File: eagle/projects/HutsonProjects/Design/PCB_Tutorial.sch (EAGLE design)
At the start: 1 part

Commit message: adding parts
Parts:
- added C1: 0.1uF, SparkFun-Capacitors:0.1UF-0603-25V-(+80/-20%)
- added J1: POWER_JACKPTH_BREAD, SparkFun-Connectors:POWER_JACKPTH_BREAD
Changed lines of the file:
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@@
 <parts>
 <part name="FRAME1" library="SparkFun-Aesthetics" deviceset="FRAME-LETTER" device=""/>
+<part name="J1" library="SparkFun-Connectors" deviceset="POWER_JACK" device="PTH_BREAD"/>
+<part name="C1" library="SparkFun-Capacitors" deviceset="0.1UF" device="-0603-25V-(+80/-20%)" value="0.1uF"/>
+<part name="SUPPLY1" library="SparkFun-PowerSymbols" deviceset="VCC" device=""/>
+<part name="GND1" library="SparkFun-PowerSymbols" deviceset="GND" device=""/>
+<part name="GND2" library="SparkFun-PowerSymbols" deviceset="GND" device=""/>
 </parts>
 <sheets>
@@
 <attribute name="REV" x="53.34" y="-51.816" size="2.7432" layer="94" font="vector"/>
 </instance>
+<instance part="J1" gate="G$1" x="-162.56" y="81.28" smashed="yes">
+<attribute name="VALUE" x="-172.72" y="91.44" size="1.778" layer="96" font="vector"/>
+<attribute name="NAME" x="-172.72" y="81.28" size="1.778" layer="95" font="vector"/>
+</instance>
+<instance part="C1" gate="G$1" x="-127" y="81.28" smashed="yes">
+<attribute name="NAME" x="-125.476" y="84.201" size="1.778" layer="95" font="vector"/>
+<attribute name="VALUE" x="-125.476" y="79.121" size="1.778" layer="96" font="vector"/>
+</instance>
+<instance part="SUPPLY1" gate="G$1" x="-132.08" y="101.6" smashed="yes">
+<attribute name="VALUE" x="-132.08" y="104.394" size="1.778" layer="96" align="bottom-center"/>
+</instance>
+<instance part="GND1" gate="1" x="-160.02" y="66.04" smashed="yes">
+<attribute name="VALUE" x="-160.02" y="65.786" size="1.778" layer="96" align="top-center"/>
+</instance>
+<instance part="GND2" gate="1" x="-144.78" y="66.04" smashed="yes">
+<attribute name="VALUE" x="-144.78" y="65.786" size="1.778" layer="96" align="top-center"/>
+</instance>
 </instances>

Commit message: adding parts
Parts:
- added C2: 0.1uF, SparkFun-Capacitors:0.1UF-KIT-EZ-50V-20%
- added D1, D2, D3: (no value), SparkFun-LED:LED5MM
- added R1, R2, R3, R4: (no value), SparkFun-Resistors:RESISTORAXIAL-0.3
- added U1: 328P, SparkFun-IC-Microcontroller:ATMEGA328P_PDIP
- C1: device SparkFun-Capacitors:0.1UF-0603-25V-(+80/-20%) -> SparkFun-Capacitors:0.1UF-KIT-EZ-50V-20%
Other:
- moved on the sheet: C1
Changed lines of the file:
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@@
 <part name="FRAME1" library="SparkFun-Aesthetics" deviceset="FRAME-LETTER" device=""/>
 <part name="J1" library="SparkFun-Connectors" deviceset="POWER_JACK" device="PTH_BREAD"/>
-<part name="C1" library="SparkFun-Capacitors" deviceset="0.1UF" device="-0603-25V-(+80/-20%)" value="0.1uF"/>
 <part name="SUPPLY1" library="SparkFun-PowerSymbols" deviceset="VCC" device=""/>
 <part name="GND1" library="SparkFun-PowerSymbols" deviceset="GND" device=""/>
 <part name="GND2" library="SparkFun-PowerSymbols" deviceset="GND" device=""/>
+<part name="U1" library="SparkFun-IC-Microcontroller" deviceset="ATMEGA328P_PDIP" device="" value="328P"/>
+<part name="R1" library="SparkFun-Resistors" deviceset="RESISTOR" device="AXIAL-0.3" value=" "/>
+<part name="R2" library="SparkFun-Resistors" deviceset="RESISTOR" device="AXIAL-0.3" value=" "/>
+<part name="R3" library="SparkFun-Resistors" deviceset="RESISTOR" device="AXIAL-0.3" value=" "/>
+<part name="R4" library="SparkFun-Resistors" deviceset="RESISTOR" device="AXIAL-0.3" value=" "/>
+<part name="C1" library="SparkFun-Capacitors" deviceset="0.1UF" device="-KIT-EZ-50V-20%" value="0.1uF"/>
+<part name="D1" library="SparkFun-LED" deviceset="LED" device="5MM"/>
+<part name="D2" library="SparkFun-LED" deviceset="LED" device="5MM"/>
+<part name="D3" library="SparkFun-LED" deviceset="LED" device="5MM"/>
+<part name="C2" library="SparkFun-Capacitors" deviceset="0.1UF" device="-KIT-EZ-50V-20%" value="0.1uF"/>
 </parts>
 <sheets>
@@
 <attribute name="NAME" x="-172.72" y="81.28" size="1.778" layer="95" font="vector"/>
 </instance>
-<instance part="C1" gate="G$1" x="-127" y="81.28" smashed="yes">
-<attribute name="NAME" x="-125.476" y="84.201" size="1.778" layer="95" font="vector"/>
-<attribute name="VALUE" x="-125.476" y="79.121" size="1.778" layer="96" font="vector"/>
-</instance>
 <instance part="SUPPLY1" gate="G$1" x="-132.08" y="101.6" smashed="yes">
 <attribute name="VALUE" x="-132.08" y="104.394" size="1.778" layer="96" align="bottom-center"/>
@@
 <attribute name="VALUE" x="-144.78" y="65.786" size="1.778" layer="96" align="top-center"/>
 </instance>
+<instance part="U1" gate="U1" x="-88.9" y="60.96" smashed="yes">
+<attribute name="NAME" x="-106.68" y="89.662" size="1.778" layer="95"/>
+<attribute name="VALUE" x="-106.68" y="22.86" size="1.778" layer="96"/>
+</instance>
+<instance part="R1" gate="G$1" x="-48.26" y="93.98" smashed="yes">
+<attribute name="NAME" x="-48.26" y="95.504" size="1.778" layer="95" font="vector" align="bottom-center"/>
+<attribute name="VALUE" x="-48.26" y="92.456" size="1.778" layer="96" font="vector" align="top-center"/>
+</instance>
+<instance part="R2" gate="G$1" x="-25.4" y="93.98" smashed="yes">
+<attribute name="NAME" x="-25.4" y="95.504" size="1.778" layer="95" font="vector" align="bottom-center"/>
+<attribute name="VALUE" x="-25.4" y="92.456" size="1.778" layer="96" font="vector" align="top-center"/>
+</instance>
+<instance part="R3" gate="G$1" x="-17.78" y="81.28" smashed="yes">
+<attribute name="NAME" x="-17.78" y="82.804" size="1.778" layer="95" font="vector" align="bottom-center"/>
+<attribute name="VALUE" x="-17.78" y="79.756" size="1.778" layer="96" font="vector" align="top-center"/>
+</instance>
+<instance part="R4" gate="G$1" x="12.7" y="101.6" smashed="yes">
+<attribute name="NAME" x="12.7" y="103.124" size="1.778" layer="95" font="vector" align="bottom-center"/>
+<attribute name="VALUE" x="12.7" y="100.076" size="1.778" layer="96" font="vector" align="top-center"/>
+</instance>
+<instance part="C1" gate="G$1" x="-129.54" y="73.66" smashed="yes">
+<attribute name="NAME" x="-128.016" y="76.581" size="1.778" layer="95" font="vector"/>
+<attribute name="VALUE" x="-128.016" y="71.501" size="1.778" layer="96" font="vector"/>
+</instance>
+<instance part="D1" gate="D1" x="-22.86" y="45.72" smashed="yes">
+<attribute name="NAME" x="-26.289" y="41.148" size="1.778" layer="95" font="vector" rot="R90"/>
+<attribute name="VALUE" x="-20.955" y="41.148" size="1.778" layer="96" font="vector" rot="R90" align="top-left"/>
+</instance>
+<instance part="D2" gate="D1" x="-10.16" y="45.72" smashed="yes">
+<attribute name="NAME" x="-13.589" y="41.148" size="1.778" layer="95" font="vector" rot="R90"/>
+<attribute name="VALUE" x="-8.255" y="41.148" size="1.778" layer="96" font="vector" rot="R90" align="top-left"/>
+</instance>
+<instance part="D3" gate="D1" x="0" y="48.26" smashed="yes">
+<attribute name="NAME" x="-3.429" y="43.688" size="1.778" layer="95" font="vector" rot="R90"/>
+<attribute name="VALUE" x="1.905" y="43.688" size="1.778" layer="96" font="vector" rot="R90" align="top-left"/>
+</instance>
+<instance part="C2" gate="G$1" x="-121.92" y="93.98" smashed="yes">
+<attribute name="NAME" x="-120.396" y="96.901" size="1.778" layer="95" font="vector"/>
+<attribute name="VALUE" x="-120.396" y="91.821" size="1.778" layer="96" font="vector"/>
+</instance>
 </instances>

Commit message: adding parts
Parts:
- added J2: (no value), SparkFun-Connectors:CONN_08"
- added J3: AVR_SPI_PROG_3X2PTH, SparkFun-Connectors:AVR_SPI_PROG_3X2PTH
- added J4: 6_PIN_SERIAL_CABLEPTH, SparkFun-Connectors:6_PIN_SERIAL_CABLEPTH
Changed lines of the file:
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@@
 <part name="D3" library="SparkFun-LED" deviceset="LED" device="5MM"/>
 <part name="C2" library="SparkFun-Capacitors" deviceset="0.1UF" device="-KIT-EZ-50V-20%" value="0.1uF"/>
+<part name="SUPPLY2" library="SparkFun-PowerSymbols" deviceset="VCC" device=""/>
+<part name="GND3" library="SparkFun-PowerSymbols" deviceset="GND" device=""/>
+<part name="SUPPLY3" library="SparkFun-PowerSymbols" deviceset="VCC" device=""/>
+<part name="GND4" library="SparkFun-PowerSymbols" deviceset="GND" device=""/>
+<part name="GND5" library="SparkFun-PowerSymbols" deviceset="GND" device=""/>
+<part name="GND6" library="SparkFun-PowerSymbols" deviceset="GND" device=""/>
+<part name="J2" library="SparkFun-Connectors" deviceset="CONN_08" device="&quot;"/>
+<part name="J3" library="SparkFun-Connectors" deviceset="AVR_SPI_PROG_3X2" device="PTH"/>
+<part name="J4" library="SparkFun-Connectors" deviceset="6_PIN_SERIAL_CABLE" device="PTH"/>
+<part name="SUPPLY4" library="SparkFun-PowerSymbols" deviceset="VCC" device=""/>
+<part name="SUPPLY5" library="SparkFun-PowerSymbols" deviceset="VCC" device=""/>
+<part name="GND7" library="SparkFun-PowerSymbols" deviceset="GND" device=""/>
+<part name="GND8" library="SparkFun-PowerSymbols" deviceset="GND" device=""/>
 </parts>
 <sheets>
@@
 <attribute name="VALUE" x="-120.396" y="91.821" size="1.778" layer="96" font="vector"/>
 </instance>
+<instance part="SUPPLY2" gate="G$1" x="-106.68" y="104.14" smashed="yes">
+<attribute name="VALUE" x="-106.68" y="106.934" size="1.778" layer="96" align="bottom-center"/>
+</instance>
+<instance part="GND3" gate="1" x="-154.94" y="40.64" smashed="yes">
+<attribute name="VALUE" x="-154.94" y="40.386" size="1.778" layer="96" align="top-center"/>
+</instance>
+<instance part="SUPPLY3" gate="G$1" x="-96.52" y="104.14" smashed="yes">
+<attribute name="VALUE" x="-96.52" y="106.934" size="1.778" layer="96" align="bottom-center"/>
+</instance>
+<instance part="GND4" gate="1" x="-147.32" y="48.26" smashed="yes">
+<attribute name="VALUE" x="-147.32" y="48.006" size="1.778" layer="96" align="top-center"/>
+</instance>
+<instance part="GND5" gate="1" x="-137.16" y="48.26" smashed="yes">
+<attribute name="VALUE" x="-137.16" y="48.006" size="1.778" layer="96" align="top-center"/>
+</instance>
+<instance part="GND6" gate="1" x="-142.24" y="40.64" smashed="yes">
+<attribute name="VALUE" x="-142.24" y="40.386" size="1.778" layer="96" align="top-center"/>
+</instance>
+<instance part="J2" gate="G$1" x="40.64" y="83.82" smashed="yes" rot="R180">
+<attribute name="VALUE" x="45.72" y="96.266" size="1.778" layer="96" font="vector" rot="R180"/>
+<attribute name="NAME" x="45.72" y="70.612" size="1.778" layer="95" font="vector" rot="R180"/>
+</instance>
+<instance part="J3" gate="G$1" x="33.02" y="48.26" smashed="yes" rot="R180">
+<attribute name="NAME" x="38.1" y="42.672" size="1.778" layer="95" font="vector" rot="R180"/>
+<attribute name="VALUE" x="38.1" y="55.626" size="1.778" layer="96" font="vector" rot="R180"/>
+</instance>
+<instance part="J4" gate="G$1" x="50.8" y="25.4" smashed="yes" rot="R180">
+<attribute name="VALUE" x="55.88" y="35.306" size="1.778" layer="96" font="vector" rot="R180"/>
+<attribute name="NAME" x="55.88" y="14.732" size="1.778" layer="95" font="vector" rot="R180"/>
+</instance>
+<instance part="SUPPLY4" gate="G$1" x="-121.92" y="104.14" smashed="yes">
+<attribute name="VALUE" x="-121.92" y="106.934" size="1.778" layer="96" align="bottom-center"/>
+</instance>
+<instance part="SUPPLY5" gate="G$1" x="-88.9" y="106.68" smashed="yes">
+<attribute name="VALUE" x="-88.9" y="109.474" size="1.778" layer="96" align="bottom-center"/>
+</instance>
+<instance part="GND7" gate="1" x="-170.18" y="66.04" smashed="yes">
+<attribute name="VALUE" x="-170.18" y="65.786" size="1.778" layer="96" align="top-center"/>
+</instance>
+<instance part="GND8" gate="1" x="-134.62" y="58.42" smashed="yes">
+<attribute name="VALUE" x="-134.62" y="58.166" size="1.778" layer="96" align="top-center"/>
+</instance>
 </instances>

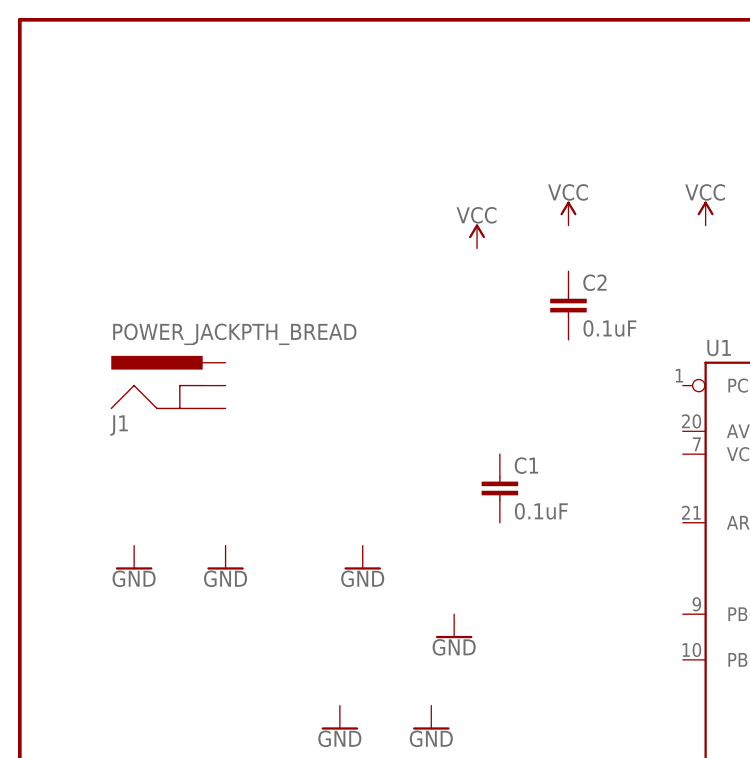
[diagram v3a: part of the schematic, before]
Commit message: Wiring up tutorial through hole circuit
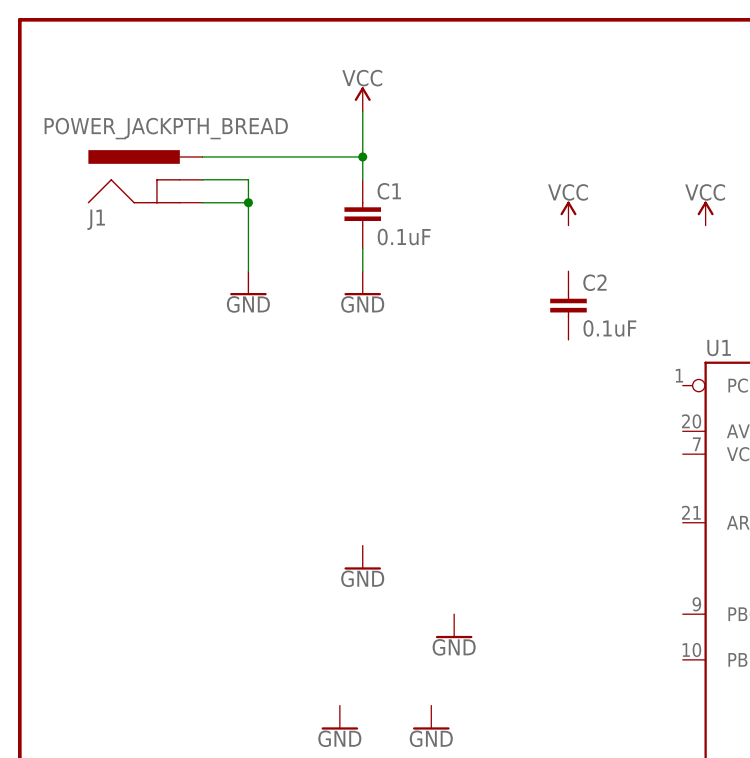
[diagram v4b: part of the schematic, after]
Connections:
- new net GND: C1.2, J1.GND, J1.GNDBREAK
- new net VCC: C1.1, J1.PWR
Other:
- moved on the sheet: C1, J1
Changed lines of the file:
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@@
 <attribute name="REV" x="53.34" y="-51.816" size="2.7432" layer="94" font="vector"/>
 </instance>
-<instance part="J1" gate="G$1" x="-162.56" y="81.28" smashed="yes">
-<attribute name="VALUE" x="-172.72" y="91.44" size="1.778" layer="96" font="vector"/>
-<attribute name="NAME" x="-172.72" y="81.28" size="1.778" layer="95" font="vector"/>
+<instance part="J1" gate="G$1" x="-165.1" y="104.14" smashed="yes">
+<attribute name="VALUE" x="-180.34" y="114.3" size="1.778" layer="96" font="vector"/>
+<attribute name="NAME" x="-175.26" y="104.14" size="1.778" layer="95" font="vector"/>
 </instance>
-<instance part="SUPPLY1" gate="G$1" x="-132.08" y="101.6" smashed="yes">
-<attribute name="VALUE" x="-132.08" y="104.394" size="1.778" layer="96" align="bottom-center"/>
+<instance part="SUPPLY1" gate="G$1" x="-144.78" y="116.84" smashed="yes">
+<attribute name="VALUE" x="-144.78" y="119.634" size="1.778" layer="96" align="bottom-center"/>
 </instance>
-<instance part="GND1" gate="1" x="-160.02" y="66.04" smashed="yes">
-<attribute name="VALUE" x="-160.02" y="65.786" size="1.778" layer="96" align="top-center"/>
+<instance part="GND1" gate="1" x="-157.48" y="96.52" smashed="yes">
+<attribute name="VALUE" x="-157.48" y="96.266" size="1.778" layer="96" align="top-center"/>
 </instance>
 <instance part="GND2" gate="1" x="-144.78" y="66.04" smashed="yes">
@@
 <attribute name="VALUE" x="12.7" y="100.076" size="1.778" layer="96" font="vector" align="top-center"/>
 </instance>
-<instance part="C1" gate="G$1" x="-129.54" y="73.66" smashed="yes">
-<attribute name="NAME" x="-128.016" y="76.581" size="1.778" layer="95" font="vector"/>
-<attribute name="VALUE" x="-128.016" y="71.501" size="1.778" layer="96" font="vector"/>
+<instance part="C1" gate="G$1" x="-144.78" y="104.14" smashed="yes">
+<attribute name="NAME" x="-143.256" y="107.061" size="1.778" layer="95" font="vector"/>
+<attribute name="VALUE" x="-143.256" y="101.981" size="1.778" layer="96" font="vector"/>
 </instance>
 <instance part="D1" gate="D1" x="-22.86" y="45.72" smashed="yes">
@@
 <attribute name="VALUE" x="-88.9" y="109.474" size="1.778" layer="96" align="bottom-center"/>
 </instance>
-<instance part="GND7" gate="1" x="-170.18" y="66.04" smashed="yes">
-<attribute name="VALUE" x="-170.18" y="65.786" size="1.778" layer="96" align="top-center"/>
+<instance part="GND7" gate="1" x="-144.78" y="96.52" smashed="yes">
+<attribute name="VALUE" x="-144.78" y="96.266" size="1.778" layer="96" align="top-center"/>
 </instance>
 <instance part="GND8" gate="1" x="-134.62" y="58.42" smashed="yes">
@@
 </busses>
 <nets>
+<net name="GND" class="0">
+<segment>
+<pinref part="J1" gate="G$1" pin="GND"/>
+<pinref part="GND1" gate="1" pin="GND"/>
+<wire x1="-162.56" y1="106.68" x2="-157.48" y2="106.68" width="0.1524" layer="91"/>
+<wire x1="-157.48" y1="106.68" x2="-157.48" y2="99.06" width="0.1524" layer="91"/>
+<pinref part="J1" gate="G$1" pin="GNDBREAK"/>
+<wire x1="-162.56" y1="109.22" x2="-157.48" y2="109.22" width="0.1524" layer="91"/>
+<wire x1="-157.48" y1="109.22" x2="-157.48" y2="106.68" width="0.1524" layer="91"/>
+<junction x="-157.48" y="106.68"/>
+</segment>
+<segment>
+<pinref part="C1" gate="G$1" pin="2"/>
+<pinref part="GND7" gate="1" pin="GND"/>
+<wire x1="-144.78" y1="101.6" x2="-144.78" y2="99.06" width="0.1524" layer="91"/>
+</segment>
+</net>
+<net name="VCC" class="0">
+<segment>
+<pinref part="J1" gate="G$1" pin="PWR"/>
+<wire x1="-162.56" y1="111.76" x2="-144.78" y2="111.76" width="0.1524" layer="91"/>
+<pinref part="C1" gate="G$1" pin="1"/>
+<wire x1="-144.78" y1="111.76" x2="-144.78" y2="109.22" width="0.1524" layer="91"/>
+<pinref part="SUPPLY1" gate="G$1" pin="VCC"/>
+<wire x1="-144.78" y1="111.76" x2="-144.78" y2="116.84" width="0.1524" layer="91"/>
+<junction x="-144.78" y="111.76"/>
+</segment>
+</net>
 </nets>
 </sheet>

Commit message: Wiring Tutorial Circuit
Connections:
- new net N$1: C2.2, R1.1, U1.PC6(/RESET)
- new net N$10: D2.C, R3.2
- new net N$11: D3.C, R4.2
- new net N$12: D3.A, U1.PB0(ICP)
- new net N$13: D2.A, U1.PB1(OC1A)
- new net N$14: D1.A, U1.PB2(SS/OC1B)
- new net N$3: J2.2, U1.PC0(ADC0)
- new net N$4: J2.3, U1.PC1(ADC1)
- new net N$5: J2.4, U1.PC2(ADC2)
- new net N$6: J2.5, U1.PC3(ADC3)
- new net N$7: J2.6, U1.PC4(ADC4/SDA)
- new net N$8: J2.7, U1.PC5(ADC5/SCL)
- new net N$9: D1.C, R2.2
- net GND: now also J2.8, R2.1, R3.1, R4.1, U1.GND
- net VCC: now also J2.1, R1.2, U1.AVCC, U1.VCC
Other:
- moved on the sheet: C2, D1, D2, D3, J2, J3, J4, R1, R2, R3, R4, U1

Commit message: Wiring Tutorial Through Hole Schematic
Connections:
- new net CTS: J4.5
- new net DTR: C2.1, J4.1
- new net RX: J4.3
- new net TX: J4.2
- net GND: now also J4.6
- net VCC: now also J4.4
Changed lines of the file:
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@@
 <wire x1="17.78" y1="0" x2="17.78" y2="-5.08" width="0.1524" layer="91"/>
+</segment>
+<segment>
+<pinref part="J4" gate="G$1" pin="6"/>
+<wire x1="-137.16" y1="60.96" x2="-121.92" y2="60.96" width="0.1524" layer="91"/>
+<label x="-124.46" y="60.96" size="1.778" layer="95"/>
 </segment>
 </net>
@@
 <pinref part="J2" gate="G$1" pin="1"/>
 <wire x1="2.54" y1="88.9" x2="7.62" y2="88.9" width="0.1524" layer="91"/>
+</segment>
+<segment>
+<pinref part="J4" gate="G$1" pin="4"/>
+<wire x1="-137.16" y1="55.88" x2="-121.92" y2="55.88" width="0.1524" layer="91"/>
+<label x="-124.46" y="55.88" size="1.778" layer="95"/>
 </segment>
 </net>
@@
 </segment>
 </net>
+<net name="CTS" class="0">
+<segment>
+<pinref part="J4" gate="G$1" pin="5"/>
+<wire x1="-137.16" y1="58.42" x2="-121.92" y2="58.42" width="0.1524" layer="91"/>
+<label x="-124.46" y="58.42" size="1.778" layer="95"/>
+</segment>
+</net>
+<net name="RX" class="0">
+<segment>
+<pinref part="J4" gate="G$1" pin="3"/>
+<wire x1="-137.16" y1="53.34" x2="-121.92" y2="53.34" width="0.1524" layer="91"/>
+<label x="-124.46" y="53.34" size="1.778" layer="95"/>
+</segment>
+</net>
+<net name="TX" class="0">
+<segment>
+<pinref part="J4" gate="G$1" pin="2"/>
+<wire x1="-137.16" y1="50.8" x2="-121.92" y2="50.8" width="0.1524" layer="91"/>
+<label x="-124.46" y="50.8" size="1.778" layer="95"/>
+</segment>
+</net>
+<net name="DTR" class="0">
+<segment>
+<pinref part="J4" gate="G$1" pin="1"/>
+<wire x1="-137.16" y1="48.26" x2="-121.92" y2="48.26" width="0.1524" layer="91"/>
+<label x="-124.46" y="48.26" size="1.778" layer="95"/>
+</segment>
+<segment>
+<pinref part="C2" gate="G$1" pin="1"/>
+<wire x1="-111.76" y1="86.36" x2="-119.38" y2="86.36" width="0.1524" layer="91"/>
+<label x="-119.38" y="86.36" size="1.778" layer="95"/>
+</segment>
+</net>
